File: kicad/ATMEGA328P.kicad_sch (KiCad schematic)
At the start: 6 parts, among them SW3 SW_Push, U3 Atmega328p-Arduino, Y1 Crystal_16MHz

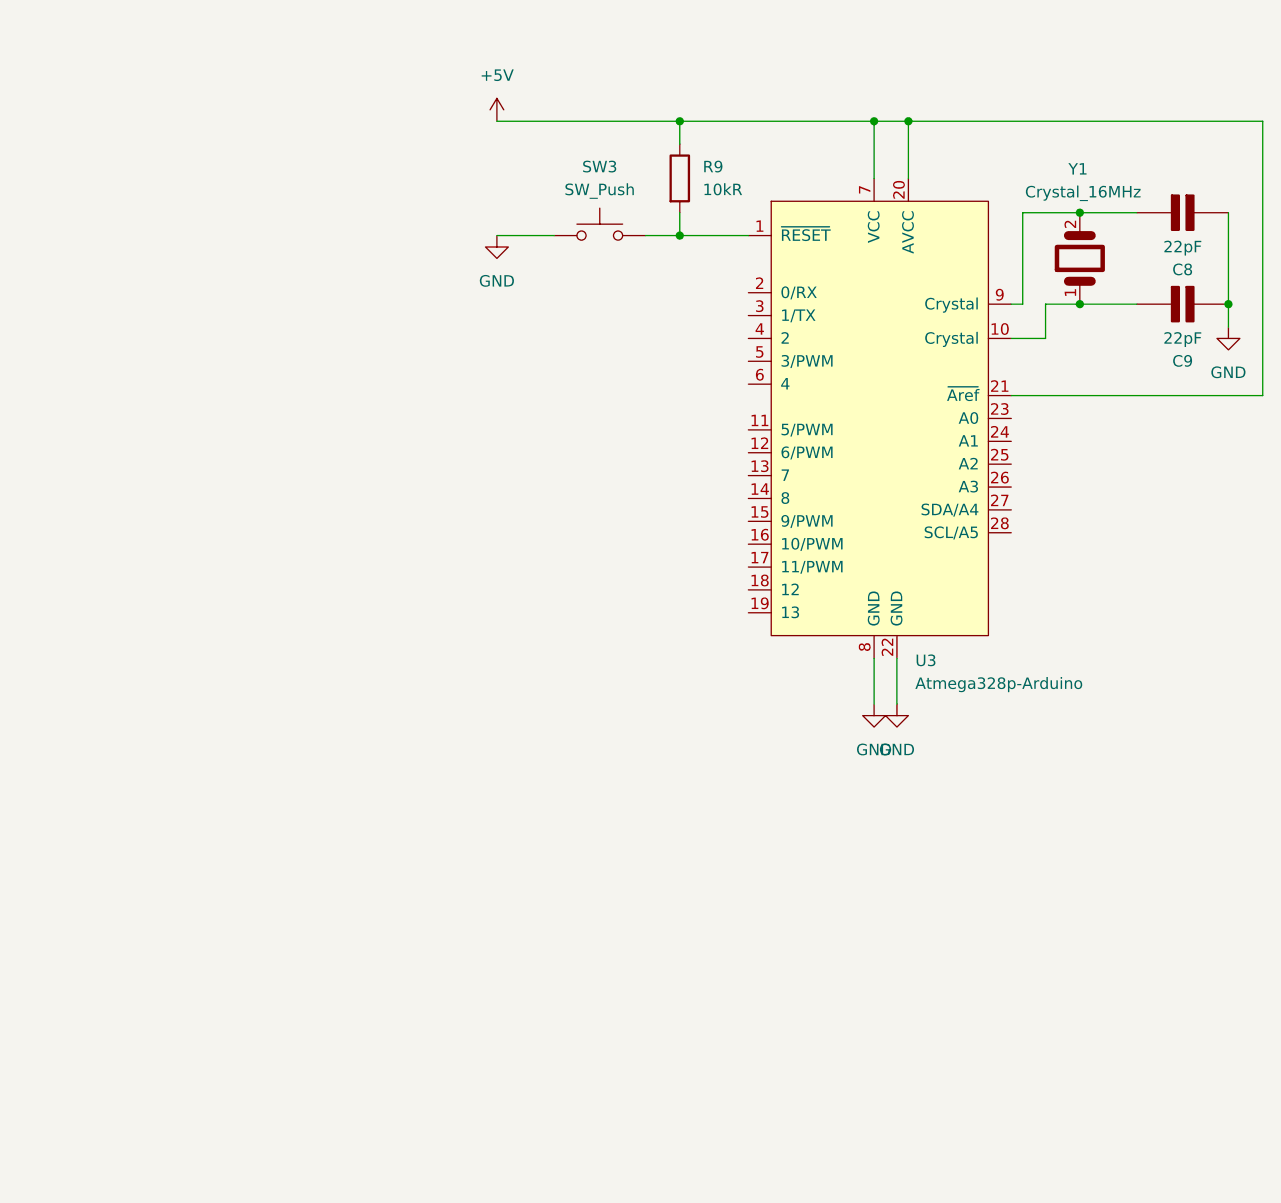
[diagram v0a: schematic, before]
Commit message: terminato collegamento ATMEGA328P
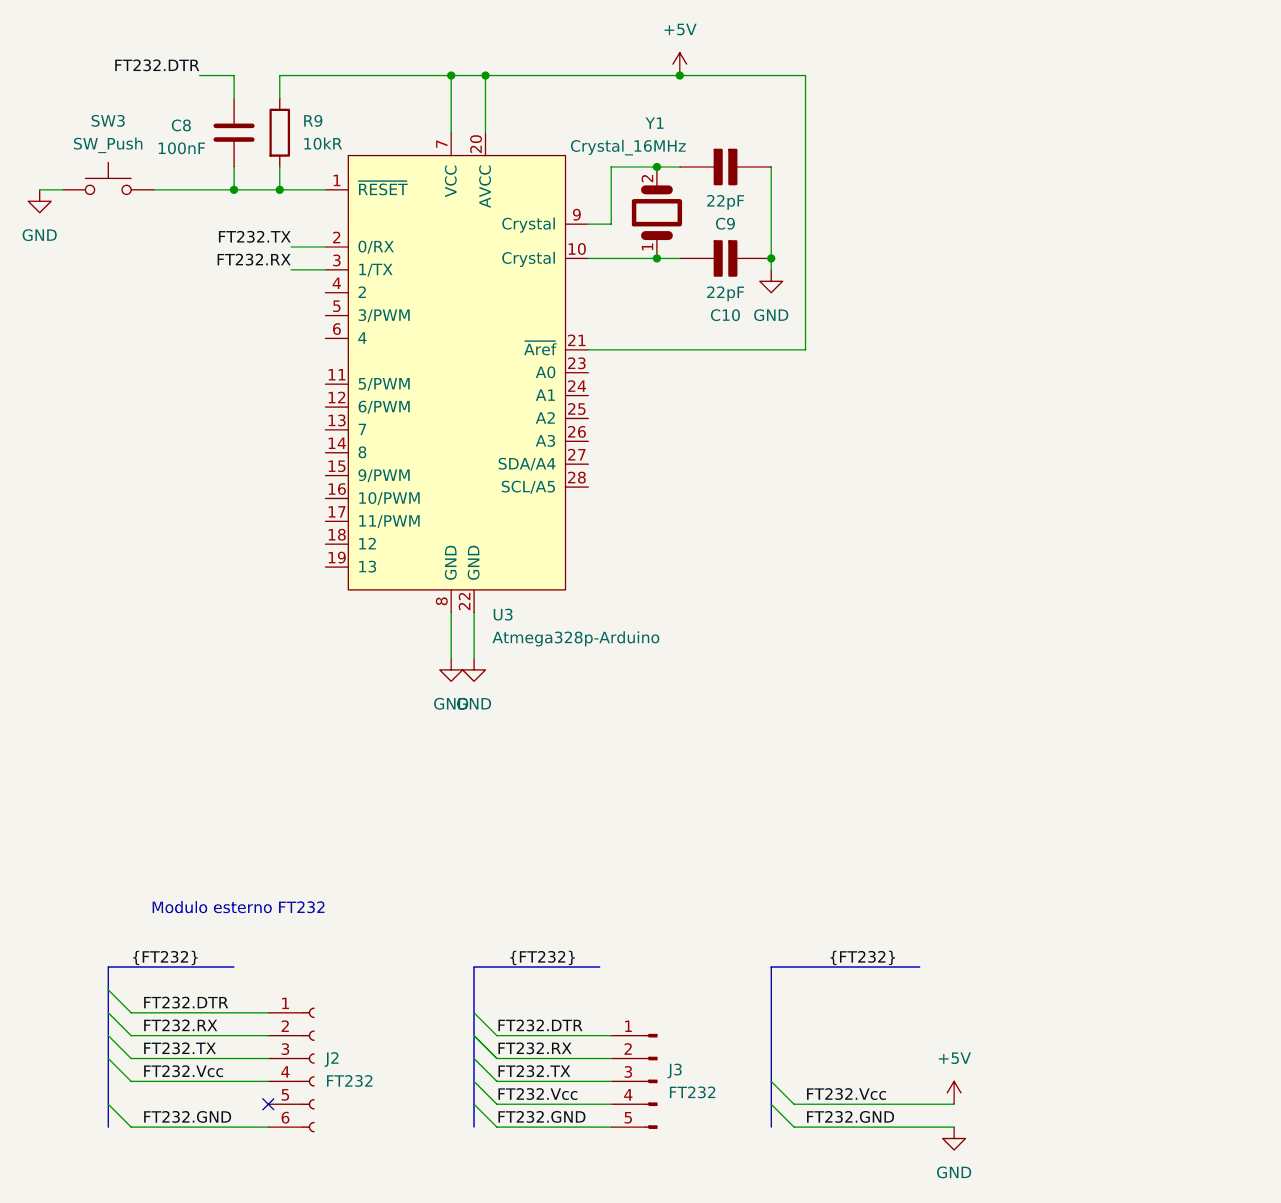
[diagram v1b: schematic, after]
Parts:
- added C8: 100nF, PCM_Capacitor_THT_AKL:C_Disc_D5.0mm_W2.5mm_P5.00mm, symbol PCM_Capacitor_AKL:C_Disc_D5.0mm_W2.5mm_P5.00mm
- added J2: FT232, symbol Connector:Conn_01x06_Socket
- added J3: FT232, symbol Connector:Conn_01x05_Pin
- renumbered C9 to C10, C8 to C9
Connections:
- net +5V: now also J2.4 (Pin_4), J3.4 (Pin_4)
- net GND: now also J2.6 (Pin_6), J3.5 (Pin_5)
- net at R9.2, SW3.2, U3.1 (~{RESET}): now also C8.1
- net FT232.TX: now reaches U3.2 (0/RX)
- net FT232.TX: now also J2.3 (Pin_3), J3.3 (Pin_3)
- net FT232.RX: now reaches U3.3 (1/TX)
- net FT232.RX: now also J2.2 (Pin_2), J3.2 (Pin_2)
- new net FT232.DTR: C8.2, J2.1 (Pin_1), J3.1 (Pin_1)
- no-connect marks 0 -> 1
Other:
- note added: "Modulo esterno FT232"
- moved on the sheet: C10, C9, R9, SW3, U3, Y1
